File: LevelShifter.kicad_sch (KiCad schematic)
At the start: 3 parts, among them Q2 BSS138

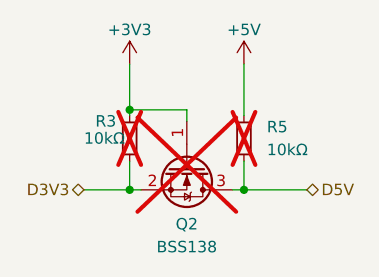
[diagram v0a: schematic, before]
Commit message: Reset usage of flag "do not place"
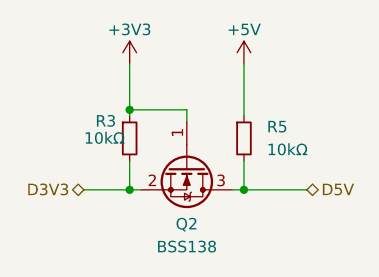
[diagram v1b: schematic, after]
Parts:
- Q2, R3, R5: now fitted
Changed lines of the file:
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@@
   )
   (symbol (lib_id "Device:R_Small") (at 76.2 78.105 0) (unit 1)
-    (in_bom yes) (on_board yes) (dnp yes)
+    (in_bom yes) (on_board yes) (dnp no)
     (property "Reference" "R3" (at 72.39 76.2 0)
       (effects (font (size 1.27 1.27)) (justify left))
@@
   )
   (symbol (lib_id "Transistor_FET:BSS138") (at 82.55 81.28 270) (unit 1)
-    (in_bom yes) (on_board yes) (dnp yes) (fields_autoplaced)
+    (in_bom yes) (on_board yes) (dnp no) (fields_autoplaced)
     (property "Reference" "Q2" (at 82.55 87.63 90)
       (effects (font (size 1.27 1.27)))
@@
   )
   (symbol (lib_id "Device:R_Small") (at 88.9 78.105 0) (unit 1)
-    (in_bom yes) (on_board yes) (dnp yes) (fields_autoplaced)
+    (in_bom yes) (on_board yes) (dnp no) (fields_autoplaced)
     (property "Reference" "R5" (at 91.44 76.835 0)
       (effects (font (size 1.27 1.27)) (justify left))

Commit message: Create schematic PDF
- Define and use slim sheet template
- Define sheet values
- Rearrange schematics for printout
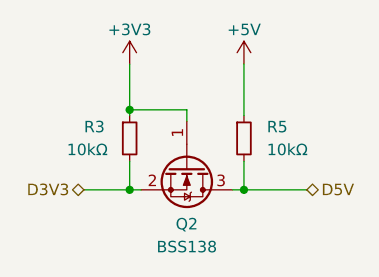
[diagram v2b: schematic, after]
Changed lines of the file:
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@@
   (symbol (lib_id "Device:R_Small") (at 76.2 78.105 0) (unit 1)
     (in_bom yes) (on_board yes) (dnp no)
-    (property "Reference" "R3" (at 72.39 76.2 0)
+    (property "Reference" "R3" (at 71.12 76.835 0)
       (effects (font (size 1.27 1.27)) (justify left))
     )
-    (property "Value" "10kΩ" (at 71.12 78.105 0)
+    (property "Value" "10kΩ" (at 69.215 79.375 0)
       (effects (font (size 1.27 1.27)) (justify left))
     )
